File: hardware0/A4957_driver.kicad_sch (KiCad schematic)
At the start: 21 parts, among them Q1 PSMN1R0-30YLC,115, Q2 PSMN1R0-30YLC,115, Q3 PSMN1R0-30YLC,115, Q4 PSMN1R0-30YLC,115

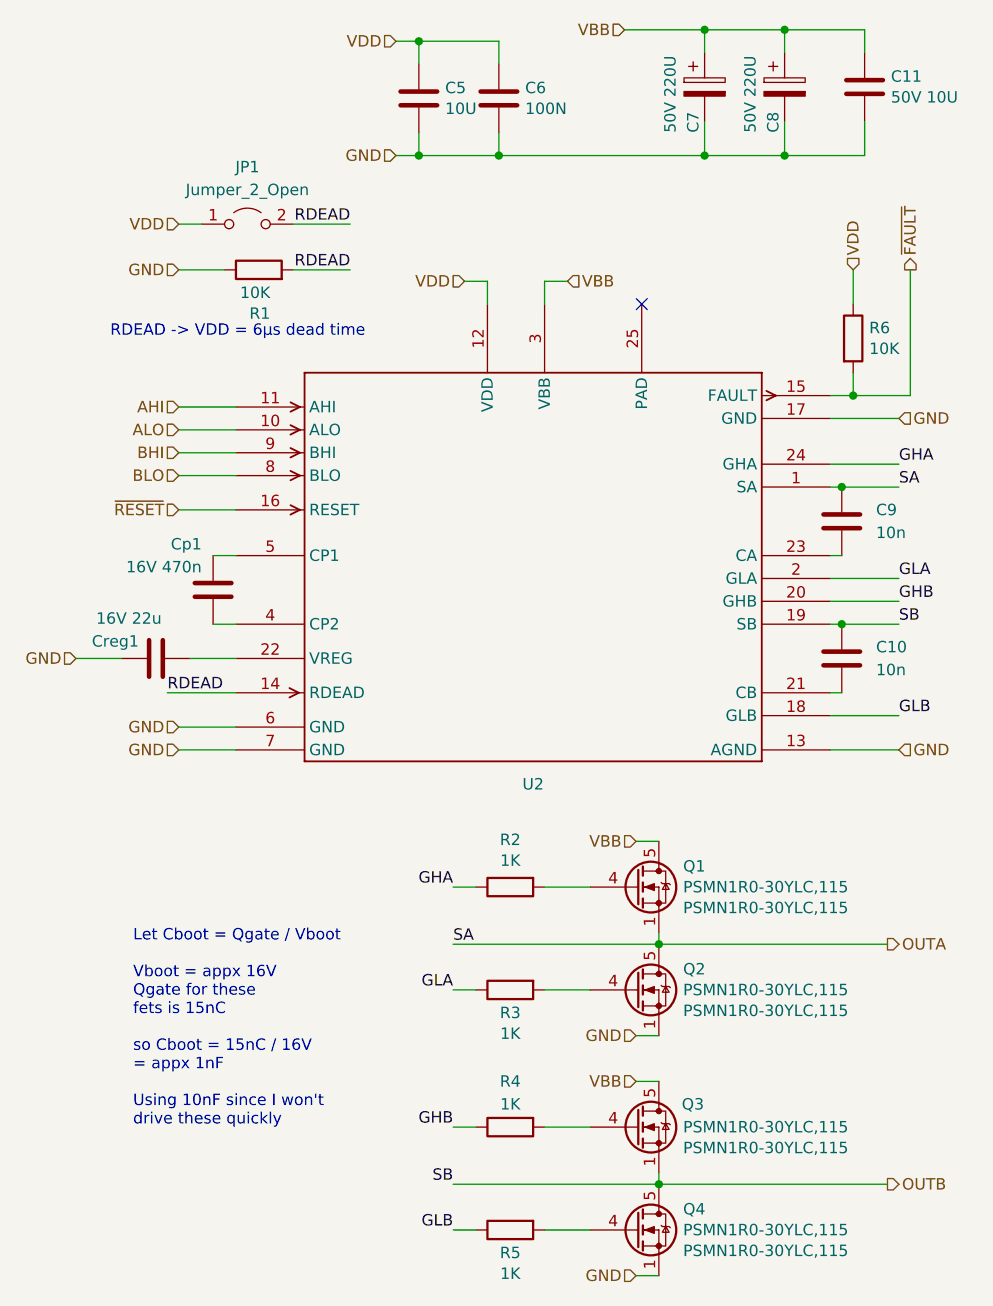
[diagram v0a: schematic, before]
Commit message: initial layout poisitions done
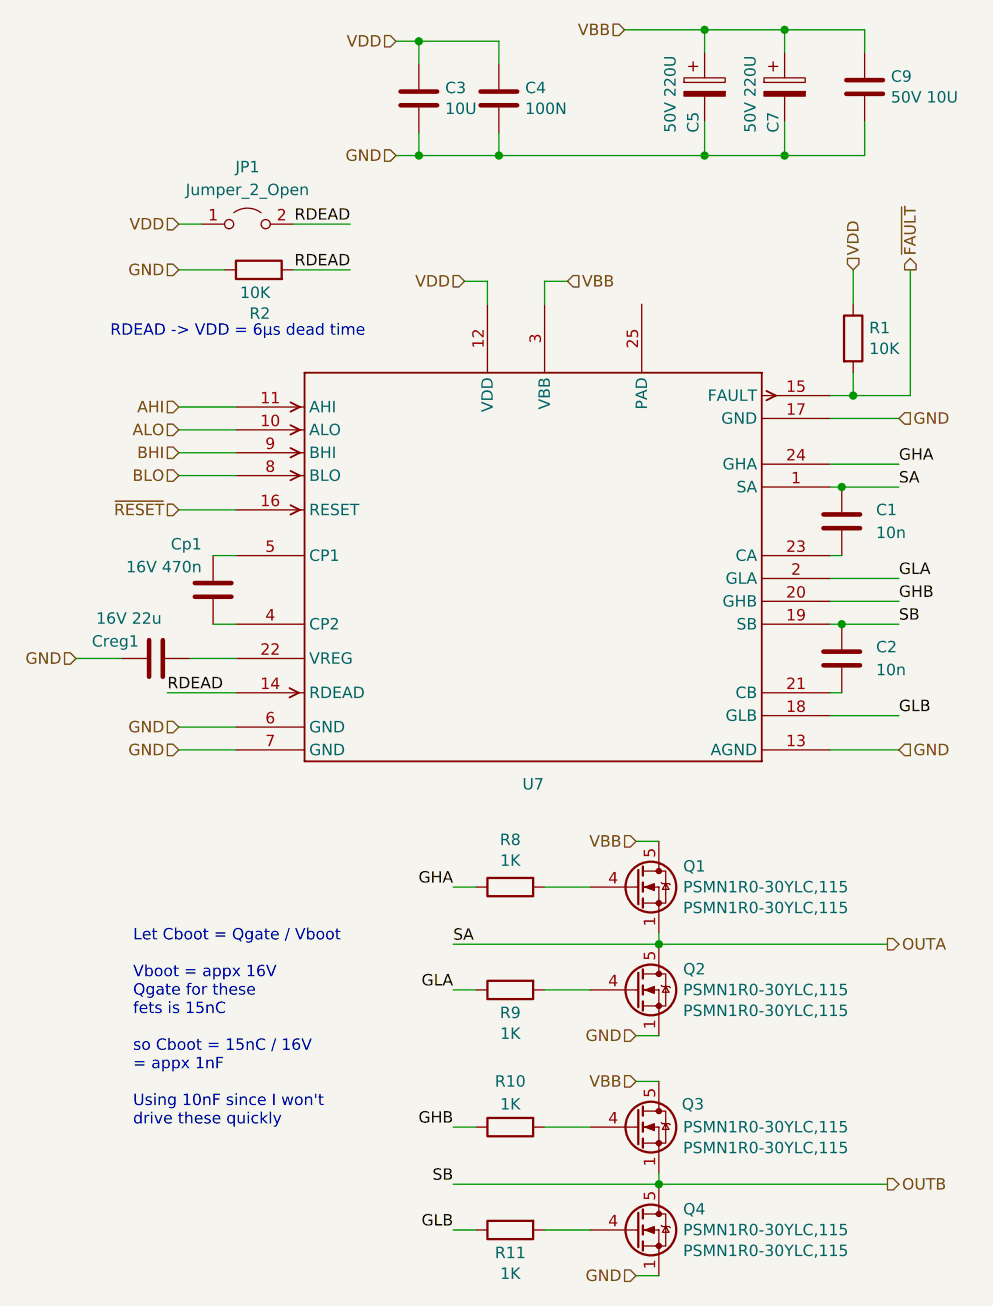
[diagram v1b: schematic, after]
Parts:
- renumbered C9 to C1, C10 to C2, C5 to C3, C6 to C4, C7 to C5, C8 to C7, C11 to C9, R6 to R1, R4 to R10, R5 to R11, R1 to R2, R2 to R8, R3 to R9, U2 to U7
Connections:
- no-connect marks 1 -> 0
